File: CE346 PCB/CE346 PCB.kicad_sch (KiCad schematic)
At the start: 56 parts, among them IC1 nRF52833-QDAA-R, J1 Conn_02x04_Odd_Even, J10 Conn_01x03_Pin, J2 Conn_01x02_Pin, J3 Conn_02x04_Odd_Even, J4 micro usb, J5 Conn_01x03_Pin, J6 micro usb, J7 Conn_01x03_Pin, J8 Conn_01x03_Pin, J9 Conn_01x03_Pin, SW1 SW_Push, SW2 SW_Push, U1 ESP32-WROOM-32E-N4, U2 SN74LV1T32DCKRG4, Y1 Crystal_GND23

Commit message: Finally added all of these files so I won't lose them again
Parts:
- removed D1, D10, D2, D3, D4, D5, D6, D7, D8, D9: D_Zener, symbol Device:D_Zener
- removed J10, J5, J7, J8, J9: Conn_01x03_Pin, symbol Connector:Conn_01x03_Pin
- removed J2: Conn_01x02_Pin, symbol Connector:Conn_01x02_Pin
- removed J4, J6: micro usb, 629105150921:WURTH_629105150921, symbol CE346 Symbols:micro usb
- removed MK1, MK2, MK3, MK4, MK5: IM69D130, CE346 Footprints:Logic_level_shifter, symbol Sensor_Audio:IM69D130
- removed R10, R11, R12, R9: 1M, symbol Device:R
- removed R17: 330, symbol Device:R
- removed R2, R3: R, symbol Device:R
- removed SW1, SW2: SW_Push, symbol Switch:SW_Push
- removed U1: ESP32-WROOM-32E-N4, symbol CE346 Symbols:ESP32-WROOM-32E-N4
- added C10, C11, C12, C29, C9: 0.1 uF, Capacitor_SMD:C_0402_1005Metric, symbol Device:C
- added C30: 4.7 uF, Capacitor_SMD:C_0805_2012Metric, symbol Device:C
- added D11, D12, D13, D14: 2.7 v Zenner, Diode_SMD:D_SOD-123, symbol Device:D_Zener
- added J11: Conn_01x06_Pin, Connector_PinHeader_2.54mm:PinHeader_1x06_P2.54mm_Vertical, symbol Connector:Conn_01x06_Pin
- added J14: Conn_01x05_Pin, Connector_PinHeader_2.54mm:PinHeader_1x05_P2.54mm_Vertical, symbol Connector:Conn_01x05_Pin
- added J15, J16, J17, J18: Conn_01x04_Pin, Connector_PinHeader_2.54mm:PinHeader_1x04_P2.54mm_Vertical, symbol Connector:Conn_01x04_Pin
- added J4: Conn_01x02_Pin, Connector_PinHeader_2.54mm:PinHeader_1x02_P2.54mm_Vertical, symbol Connector:Conn_01x02_Pin
- added J5, J6, J7, J8: Conn_01x02_Pin, symbol Connector:Conn_01x02_Pin
- added LED4: Blue, LED_SMD:LED_0603_1608Metric, symbol Device:LED
- added R19: 330, symbol Device:R
- added R20, R21, R22: 330, Resistor_SMD:R_0805_2012Metric, symbol Device:R
- added R23: 10 k, Resistor_SMD:R_0805_2012Metric, symbol Device:R
- added R24: 330R, Capacitor_SMD:C_0402_1005Metric, symbol Device:R
- added U3: ESP32-WROOM-32E-N4, symbol CE346 Symbols:ESP32-WROOM-32E-N4
- added U4: MP34DT05TR-A, MP34DT05TR-A_STM, symbol 2026-05-14_17-03-08:MP34DT05TR-A
- added U5, U6, U7, U8: SN74LV1T32DCKRG4, DCK0005A_N, symbol CE346 Symbols:SN74LV1T32DCKRG4
- added U9: LDL1117S30R, SOT223_STM, symbol 2026-04-27_01-58-37:LDL1117S30R
- C3: value C -> 100 pF; footprint (none) -> Capacitor_SMD:C_0402_1005Metric
- C4: value C -> 1.0 uF; footprint (none) -> Capacitor_SMD:C_0402_1005Metric
- C5: value C -> 100 nF; footprint (none) -> Capacitor_SMD:C_0402_1005Metric
- C6: value C -> 0.1 uF; footprint (none) -> Capacitor_SMD:C_0402_1005Metric
- C7: value C -> 820 pF; footprint (none) -> Capacitor_SMD:C_0402_1005Metric
- C8: value C -> 22 uF; footprint (none) -> Capacitor_SMD:C_0805_2012Metric
- R1: value 1M -> 10 k; footprint (none) -> Resistor_SMD:R_0805_2012Metric
- R13, R14, R15, R16: value 330 -> 1M; footprint (none) -> Resistor_SMD:R_0805_2012Metric
- R4, R5, R6, R7, R8: footprint (none) -> Resistor_SMD:R_0805_2012Metric
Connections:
- net PIEZO_1- is gone; now on net GND: J3.2 (Pin_2)
- net PIEZO_2- is gone; now on net GND: J3.4 (Pin_4)
- net PIEZO_3- is gone; now on net GND: J3.6 (Pin_6)
- net PIEZO_4- is gone; now on net GND: J3.8 (Pin_8)
- net ESP_CS: now also U3.29 (IO5)
- net GND: now also IC1.25 (VSS_PA), IC1.37 (VSS_1), IC1.41 (VSS_2), R13.1, R14.1, R15.1, R16.1, U2.2 (B), U2.3 (GND), C10.2, C11.2, C12.2, C29.1, C30.1, C9.2, D11.2 (A), D12.2 (A), D13.2 (A), D14.2 (A), J11.2 (Pin_2), J14.2 (Pin_2), J15.2 (Pin_2), J15.4 (Pin_4), J16.2 (Pin_2), J17.2 (Pin_2), J17.4 (Pin_4), J18.2 (Pin_2), J18.4 (Pin_4), J4.2 (Pin_2), J5.2 (Pin_2), J6.2 (Pin_2), J7.2 (Pin_2), J8.2 (Pin_2), LED4.1 (K), U3.1 (GND), U3.15 (GND), U3.38 (GND), U3.39 (GND), U3.40 (GND), U3.41 (GND), U3.42 (GND), U3.43 (GND), U3.44 (GND), U3.45 (GND), U3.46 (GND), U3.47 (GND), U4.2 (LR), U4.5 (GND), U5.2 (B), U5.3 (GND), U6.3 (GND), U7.3 (GND), U8.3 (GND), U9.1 (GND); no longer C4.2, J1.8 (Pin_8)
- net IR_MUX_CTRL1: now also IC1.15 (P0.17); no longer IC1.14 (P0.15), J1.2 (Pin_2)
- net IR_MUX_CTRL2: now also IC1.17 (P0.20); no longer IC1.15 (P0.17), J1.4 (Pin_4)
- net IR_MUX_CTRL3: now also IC1.31 (P0.03/AIN1); no longer IC1.17 (P0.20), J1.6 (Pin_6)
- net LED1: now also U2.4 (Y)
- net LED2: now also U5.4 (Y)
- net LED3: now also U6.4 (Y)
- net LED4: now also U7.4 (Y)
- net LED5: now also U8.4 (Y)
- net PIEZO_1+: now also R13.2, D11.1 (K), R19.1; no longer IC1.35 (P0.30/AIN6)
- net PIEZO_2+: now also R14.2, D12.1 (K), R20.1; no longer IC1.34 (P0.29/AIN5)
- net PIEZO_3+: now also R15.2, D13.1 (K), R21.1; no longer IC1.33 (P0.28/AIN4)
- net PIEZO_4+: now also R16.2, D14.1 (K), R22.1; no longer IC1.32 (P0.02/AIN0)
- net SPI_MISO: now also U3.37 (IO23)
- net SPI_MOSI: now also U3.31 (IO19)
- net SPI_SCK: now also U3.30 (IO18)
- net at R6.1: now also J8.1 (Pin_1)
- net at R4.1: now also J4.1 (Pin_1)
- net VDD3V3: now reaches R1.1
- net VDD3V3: now also C6.1, C8.1, IC1.18 (VDD_2), IC1.30 (VDD_3), IC1.40 (VDD_4), IC1.8 (VDD_1), C10.1, C11.1, C12.1, C9.1, J11.1 (Pin_1), J14.1 (Pin_1), R23.1, U3.2 (3V3), U4.1 (VDD)
- net NRST: now reaches R1.2
- net NRST: now also IC1.16 (P0.18/NRESET), J14.5 (Pin_5); no longer R13.1
- net at R5.1: now also J7.1 (Pin_1)
- net at R8.1: now also J5.1 (Pin_1)
- net DEC 4/6: now reaches C4.1, IC1.26 (DEC6)
- net DEC4/6: now reaches IC1.38 (DEC4)
- net DEC4/6: no longer C6.1
- net at IC1.11 (DECUSB): no longer C8.1
- net at R7.1: now also J6.1 (Pin_1)
- net DIN1: now reaches U2.1 (A)
- net DIN1: now also U3.27 (IO16)
- net VDD5V0: now reaches U2.5 (VCC)
- net VDD5V0: now also J16.1 (Pin_1), U5.5 (VCC), U6.5 (VCC), U7.5 (VCC), U8.5 (VCC)
- net SWDIO: now reaches IC1.19 (SWDIO)
- net SWDIO: now also J14.3 (Pin_3)
- net NRF_TX: now reaches IC1.2 (P0.00/XL1)
- net NRF_TX: now also J17.1 (Pin_1)
- net SWDCLK: now reaches IC1.20 (SWDCLK)
- net SCOREBOARD_RX: now reaches IC1.22 (P0.09/NFC1)
- net SCOREBOARD_RX: now also J15.3 (Pin_3)
- net SCOREBOARD_TX: now reaches IC1.23 (P0.10/NFC2)
- net SCOREBOARD_TX: now also J15.1 (Pin_1)
- net NRF_RX: now reaches IC1.3 (P0.01/XL2)
- net NRF_RX: now also J17.3 (Pin_3)
- new net: R23.2, U3.3 (EN)
- new net: LED4.2 (A), R24.2
- new net BCLK: J11.3 (Pin_3), U3.13 (IO14)
- new net DIN2: U3.26 (IO4), U5.1 (A)
- new net DIN3: U3.8 (IO32), U6.1 (A)
- new net DIN4: U3.9 (IO33), U7.1 (A)
- new net DIN5: U3.10 (IO25), U8.1 (A)
- new net DOUT: J11.5 (Pin_5), U3.36 (IO22)
- new net IR_MUX_CTRL0: IC1.14 (P0.15)
- new net IR_MUX_CTRL_0: J1.8 (Pin_8)
- new net IR_MUX_CTRL_1: J1.6 (Pin_6)
- new net IR_MUX_CTRL_2: J1.4 (Pin_4)
- new net IR_MUX_CTRL_3: J1.2 (Pin_2)
- new net LRCL: J11.4 (Pin_4), U3.16 (IO13)
- new net PDM_CLK: U3.12 (IO27), U4.3 (CLK)
- new net PDM_DATA: U3.11 (IO26), U4.4 (DOUT)
- new net PIEZO1: IC1.35 (P0.30/AIN6), R19.2
- new net PIEZO2: IC1.34 (P0.29/AIN5), R20.2
- new net PIEZO3: IC1.33 (P0.28/AIN4), R21.2
- new net PIEZO4: IC1.32 (P0.02/AIN0), R22.2
- new net RX0: J16.4 (Pin_4), U3.34 (RXD0)
- new net SEL: J11.6 (Pin_6), U3.28 (IO17)
- new net SWCLK: J14.4 (Pin_4)
- new net TX0: J16.3 (Pin_3), U3.35 (TXD0)
- new net UART1_RX: J18.3 (Pin_3)
- new net UART2_RX: U3.6 (IO34)
- new net UART2_TX: J18.1 (Pin_1), U3.33 (IO21)
- new net USB_5V: C29.2, U9.3 (VIN)
- new net VDD3V3_2: C30.2, R24.1, U9.2 (VOUT), U9.4 (VOUT)
- no-connect marks 0 -> 13
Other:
- note removed: "micro usb to program esp32"
- note removed: "micro usb to program nrf"
- moved on the sheet: IC1, U2

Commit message: pushing the changes
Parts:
- added J9: Conn_01x02_Pin, Connector_PinHeader_2.54mm:PinHeader_1x02_P2.54mm_Vertical, symbol Connector:Conn_01x02_Pin
- C1, C2: value C -> 12 pF; footprint (none) -> Capacitor_SMD:C_0402_1005Metric
- IC1: footprint QFN40P500X500X90-41N -> nrf:QFN40_5X5_DQ_NOR-L
- U2, U5, U6, U7, U8: footprint DCK0005A_N -> CE346 Footprints:DBV0005A_N
- U3: footprint (none) -> esp:ESP32­WROOM­32E_EXP
- U4: footprint MP34DT05TR-A_STM -> CE346 Footprints:MP34DT05TR-A_STM
- Y1: footprint (none) -> CE346 Footprints:32MHz Crystal
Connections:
- net USB_5V is gone; now on net VDD5V0: C29.2, U9.3 (VIN)
- net VDD3V3_2 is gone; now on net VDD3V3: C30.2, R24.1, U9.2 (VOUT), U9.4 (VOUT)
- net GND: now also C4.2, U6.2 (B), U7.2 (B), U8.2 (B), J9.2 (Pin_2)
- net VDD3V3: now also IC1.9 (VDDH)
- net VDD5V0: now also J9.1 (Pin_1)

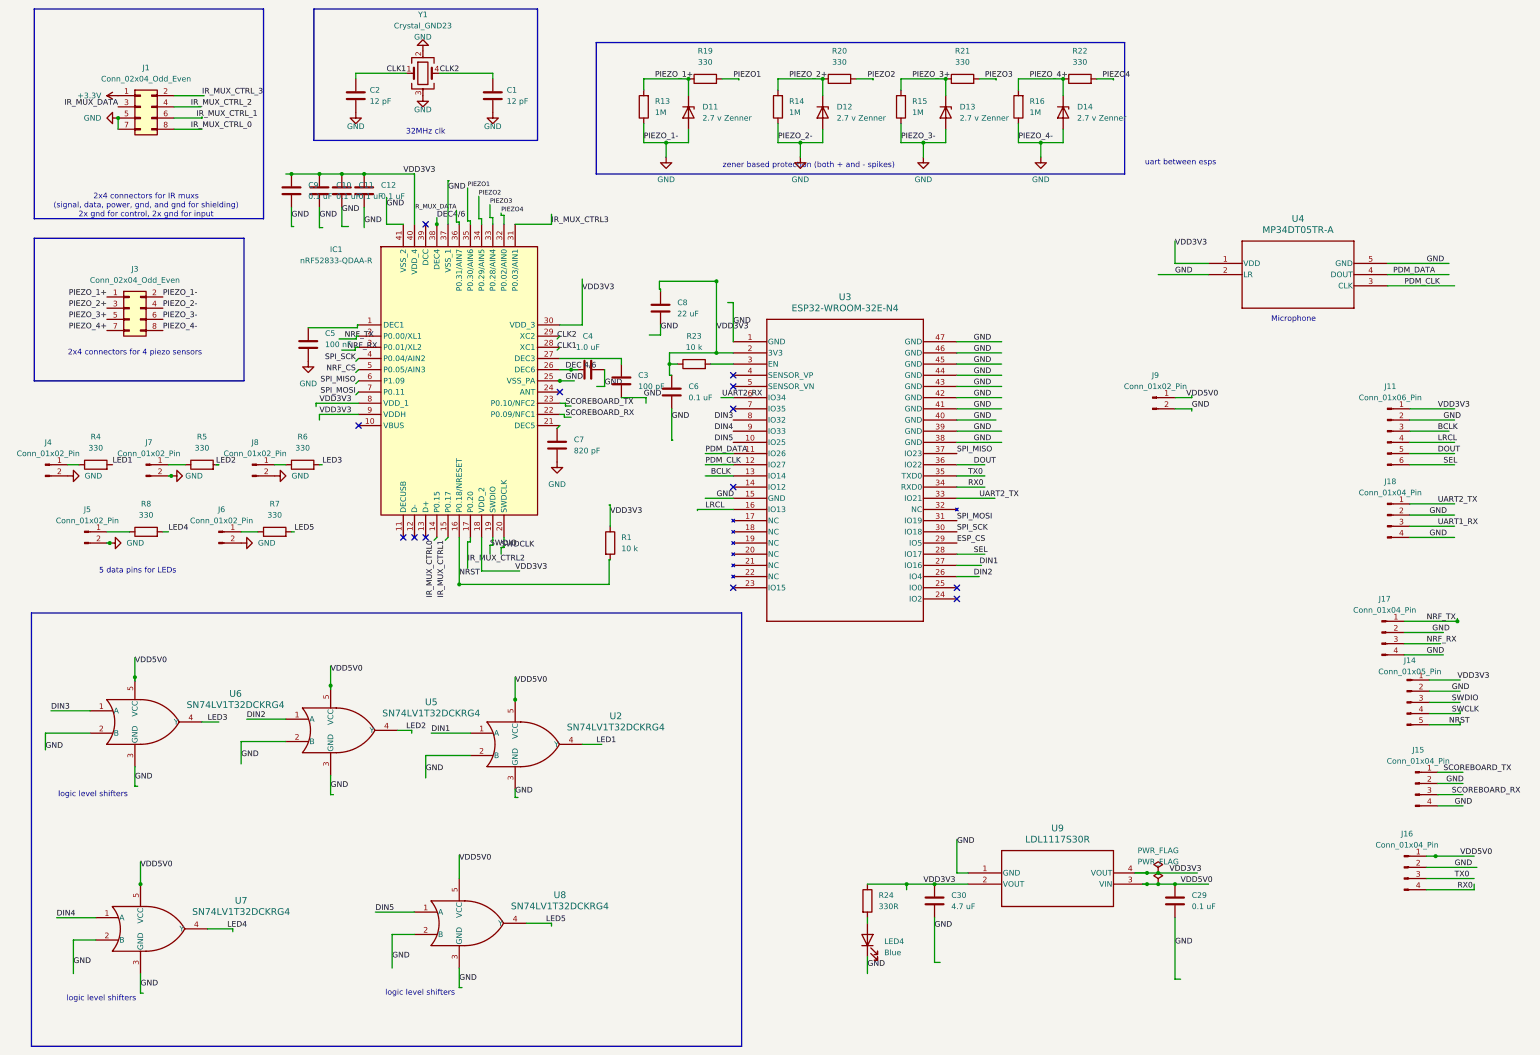
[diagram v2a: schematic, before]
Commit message: pushing the changes to the routed  PCB
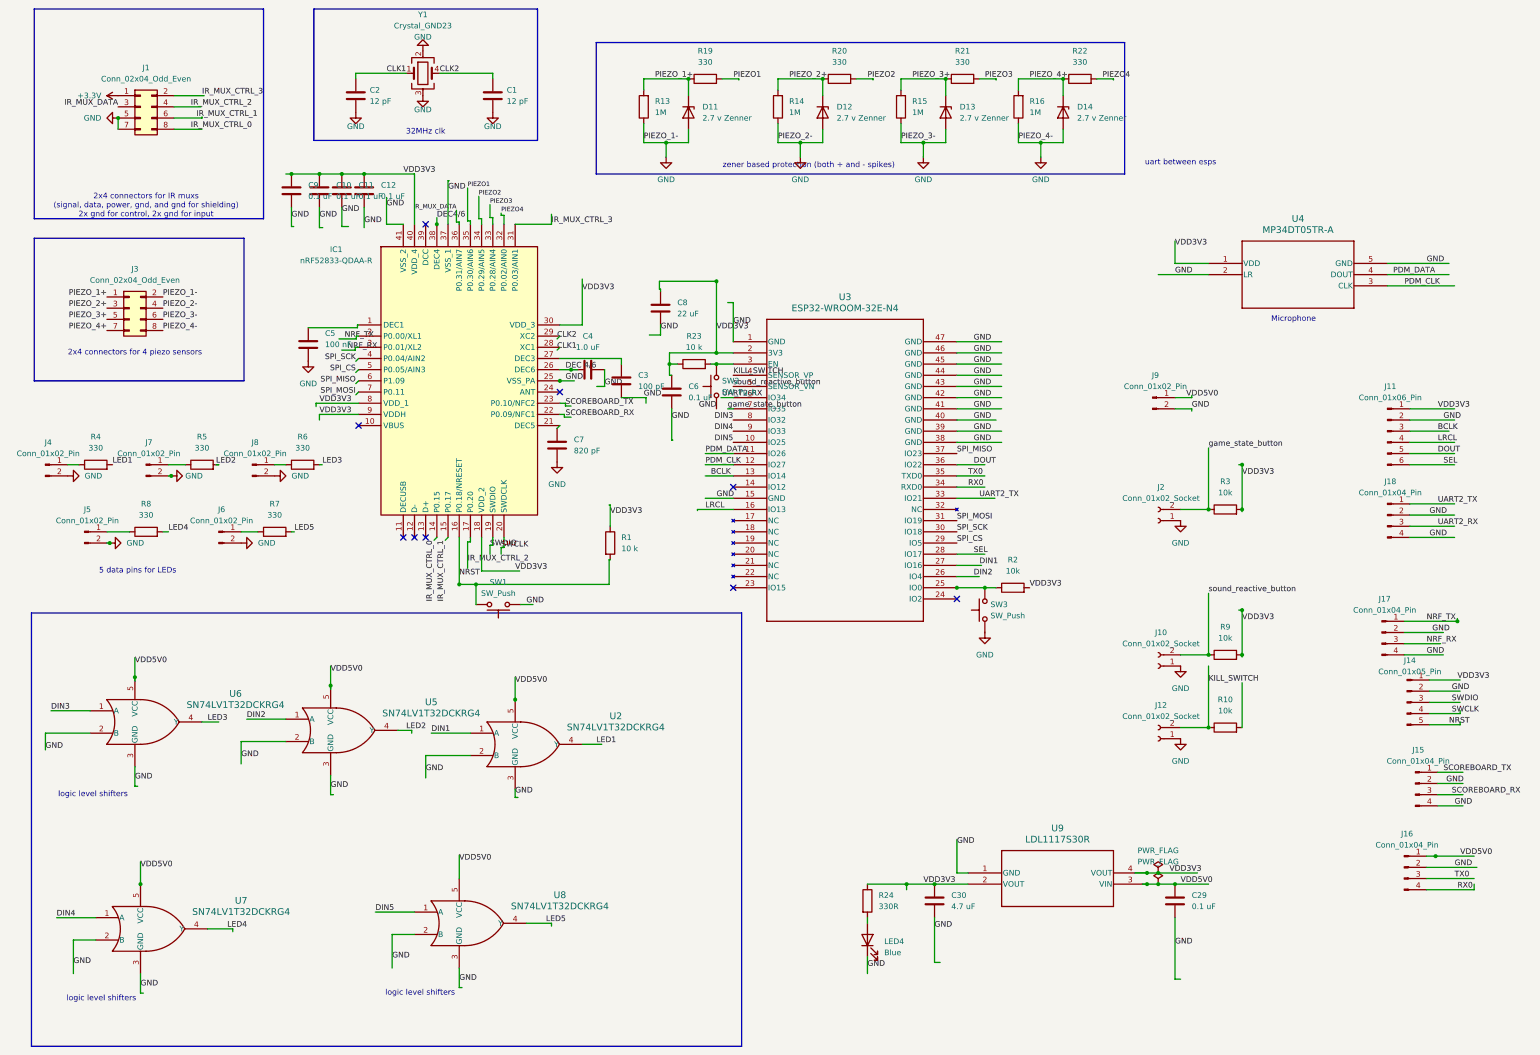
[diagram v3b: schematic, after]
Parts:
- added J10, J12, J2: Conn_01x02_Socket, Connector_PinHeader_2.54mm:PinHeader_1x02_P2.54mm_Vertical, symbol Connector:Conn_01x02_Socket
- added R10, R2, R3, R9: 10k, Resistor_SMD:R_0805_2012Metric, symbol Device:R
- added SW1, SW2, SW3: SW_Push, CE346 Footprints:pushbutton, symbol Switch:SW_Push
- J5, J6, J7, J8: footprint (none) -> Connector_PinHeader_2.54mm:PinHeader_1x02_P2.54mm_Vertical
- R19: footprint (none) -> Resistor_SMD:R_0805_2012Metric
- U9: footprint SOT223_STM -> CE346 Footprints:SOT223_STM
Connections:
- net IR_MUX_CTRL0 is gone; now on net IR_MUX_CTRL_0: IC1.14 (P0.15)
- net IR_MUX_CTRL1 is gone; now on net IR_MUX_CTRL_1: IC1.15 (P0.17)
- net IR_MUX_CTRL2 is gone; now on net IR_MUX_CTRL_2: IC1.17 (P0.20)
- net IR_MUX_CTRL3 is gone; now on net IR_MUX_CTRL_3: IC1.31 (P0.03/AIN1)
- net NRF_CS is gone; now on net SPI_CS: IC1.5 (P0.05/AIN3)
- net SWDCLK is gone; now on net SWCLK: IC1.20 (SWDCLK)
- net UART1_RX is gone; now on net UART2_RX: J18.3 (Pin_3)
- net GND: now also J10.1 (Pin_1), J12.1 (Pin_1), J2.1 (Pin_1), SW1.1, SW2.1, SW3.1
- net NRST: now also SW1.2
- net VDD3V3: now also R2.2, R3.2, R9.2
- net at U3.25 (IO0): now also R2.1, SW3.2
- net at R23.2, U3.3 (EN): now also SW2.2
- net KILL_SWITCH: now reaches U3.4 (SENSOR_VP)
- net KILL_SWITCH: now also J12.2 (Pin_2), R10.1
- net sound_reactive_button: now reaches U3.5 (SENSOR_VN)
- net sound_reactive_button: now also J10.2 (Pin_2), R9.1
- net game_state_button: now reaches U3.7 (IO35)
- net game_state_button: now also J2.2 (Pin_2), R3.1
- net ESP_CS renamed SPI_CS
- no-connect marks 13 -> 9
